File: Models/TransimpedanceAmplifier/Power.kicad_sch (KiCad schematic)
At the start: 0 parts

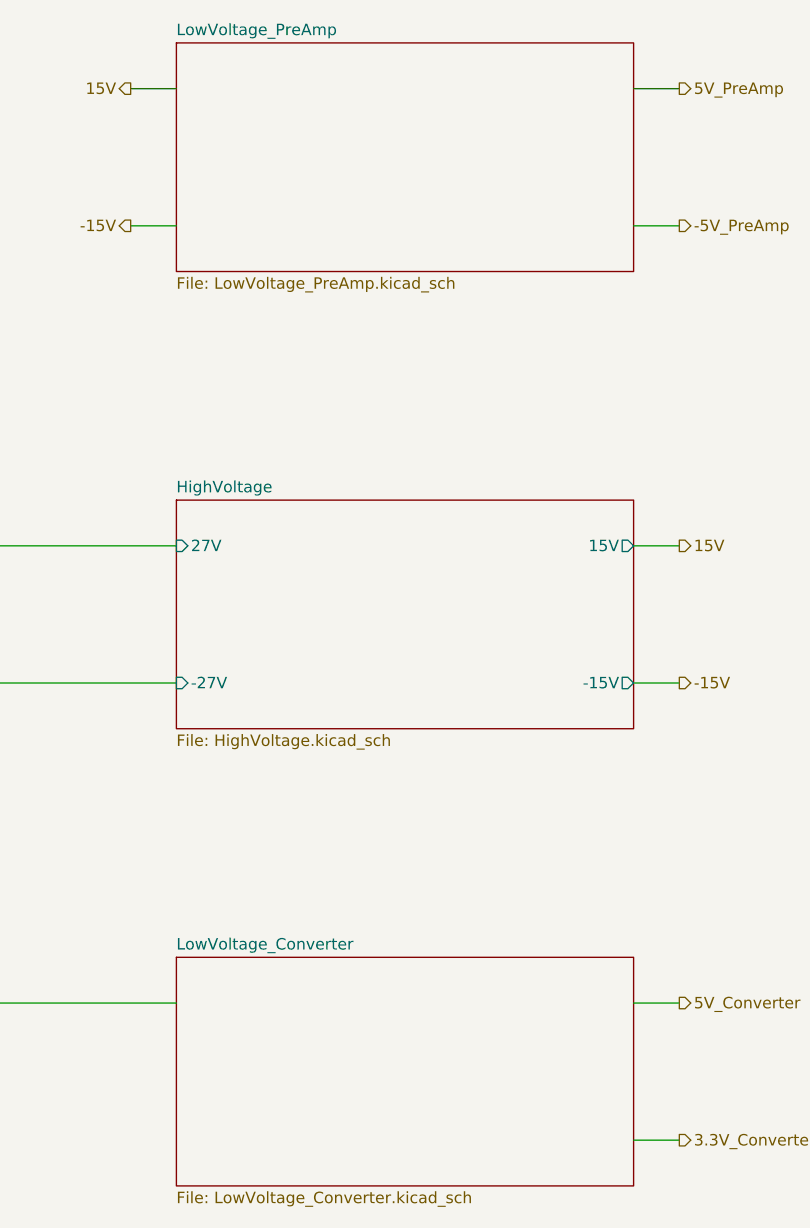
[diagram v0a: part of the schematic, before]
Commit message: Fully specified the high-level connections between subsystems
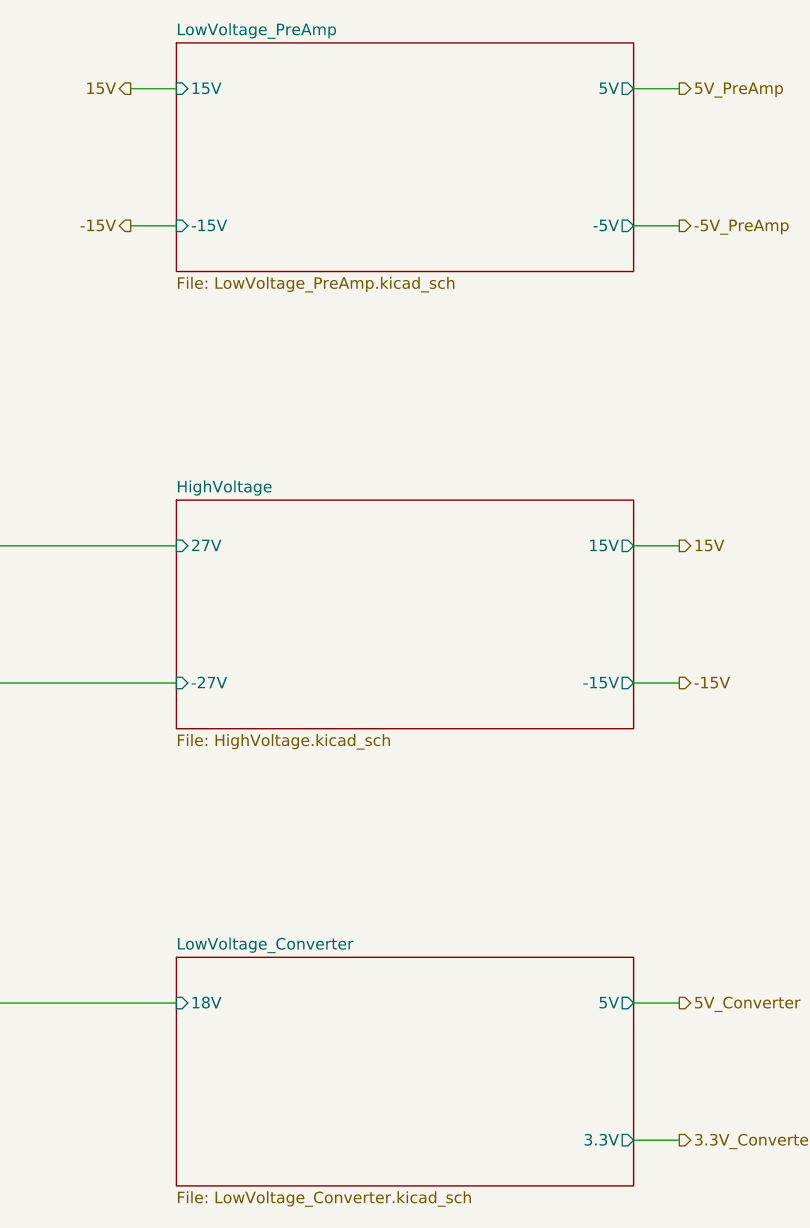
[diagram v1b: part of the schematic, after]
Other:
- sheet LowVoltage_Converter ports: added 18V, 3.3V, 5V; removed none
- sheet LowVoltage_PreAmp ports: added -15V, -5V, 15V, 5V; removed none
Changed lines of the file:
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@@
 		)
 		(instances
-			(project "TransimpedanceAmplifier"
-				(path "/ec9f2ae3-e40d-40eb-9760-2b611ee8efd1/68e8bf39-bd36-49ed-a85c-9ce753018063"
-					(page "12")
+			(project ""
+				(path "/d0ece2d4-5b22-4822-ad0c-e2361683ec3d"
+					(page "")
+				)
+			)
+			(project "TransimpedanceAmplifier"
+				(path "/ec9f2ae3-e40d-40eb-9760-2b611ee8efd1/d0ece2d4-5b22-4822-ad0c-e2361683ec3d"
+					(page "10")
 				)
 			)
@@
 			)
 		)
-		(instances
-			(project "TransimpedanceAmplifier"
-				(path "/ec9f2ae3-e40d-40eb-9760-2b611ee8efd1/68e8bf39-bd36-49ed-a85c-9ce753018063"
-					(page "16")
+		(pin "3.3V" output
+			(at 203.2 147.32 0)
+			(effects
+				(font
+					(size 1.27 1.27)
+				)
+				(justify right)
+			)
+		)
+		(pin "5V" output
+			(at 203.2 132.08 0)
+			(effects
+				(font
+					(size 1.27 1.27)
+				)
+				(justify right)
+			)
+		)
+		(pin "18V" input
+			(at 152.4 132.08 180)
+			(effects
+				(font
+					(size 1.27 1.27)
+				)
+				(justify left)
+			)
+		)
+		(instances
+			(project ""
+				(path "/d0ece2d4-5b22-4822-ad0c-e2361683ec3d"
+					(page "")
+				)
+			)
+			(project "TransimpedanceAmplifier"
+				(path "/ec9f2ae3-e40d-40eb-9760-2b611ee8efd1/d0ece2d4-5b22-4822-ad0c-e2361683ec3d"
+					(page "11")
 				)
 			)
@@
 		)
 		(instances
-			(project "TransimpedanceAmplifier"
-				(path "/ec9f2ae3-e40d-40eb-9760-2b611ee8efd1/68e8bf39-bd36-49ed-a85c-9ce753018063"
-					(page "14")
+			(project ""
+				(path "/d0ece2d4-5b22-4822-ad0c-e2361683ec3d"
+					(page "")
+				)
+			)
+			(project "TransimpedanceAmplifier"
+				(path "/ec9f2ae3-e40d-40eb-9760-2b611ee8efd1/d0ece2d4-5b22-4822-ad0c-e2361683ec3d"
+					(page "3")
 				)
 			)
@@
 			)
 		)
-		(instances
-			(project "TransimpedanceAmplifier"
-				(path "/ec9f2ae3-e40d-40eb-9760-2b611ee8efd1/68e8bf39-bd36-49ed-a85c-9ce753018063"
-					(page "15")
-				)
-			)
+		(pin "-5V" output
+			(at 203.2 45.72 0)
+			(effects
+				(font
+					(size 1.27 1.27)
+				)
+				(justify right)
+			)
+		)
+		(pin "-15V" input
+			(at 152.4 45.72 180)
+			(effects
+				(font
+					(size 1.27 1.27)
+				)
+				(justify left)
+			)
+		)
+		(pin "5V" output
+			(at 203.2 30.48 0)
+			(effects
+				(font
+					(size 1.27 1.27)
+				)
+				(justify right)
+			)
+		)
+		(pin "15V" input
+			(at 152.4 30.48 180)
+			(effects
+				(font
+					(size 1.27 1.27)
+				)
+				(justify left)
+			)
+		)
+		(instances
+			(project ""
+				(path "/d0ece2d4-5b22-4822-ad0c-e2361683ec3d"
+					(page "")
+				)
+			)
+			(project "TransimpedanceAmplifier"
+				(path "/ec9f2ae3-e40d-40eb-9760-2b611ee8efd1/d0ece2d4-5b22-4822-ad0c-e2361683ec3d"
+					(page "4")
+				)
+			)

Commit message: Syncing changes?
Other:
- note added: "Loads on Each Regulator 5 V (PreAmp) 13-17 mA 132-166 mW -5 V (PreAmp) 12-15 mA 117-153 mW 15 V 45-50 mA 616-687 mW -15 V 47-49 mA 597-650 mW 5 V (Converter) 37-40 mA 469-508 mW 3.3 V (Converter) 23 mA 49 mW"
- note added: "Maximum Permitted Power Dissipation Ambient Temperature: 30°C LM78L, TO-92 0.68 W 0.84 W (heat sinked) ~158.7°C/W (in a standard test PCB) LM78, TO-220 1.78 W 7.88 W (heat sinked) ~23.9°C/W (in a standard test PCB)"
- note removed: "TODO: Tabulate the maximum expected current at each regulator, to see whether LM78xx is needed anywhere instead of LM78Lxx"
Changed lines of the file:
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@@
 	(generator_version "9.0")
 	(paper "A4")
-	(text "TODO: Tabulate the maximum expected\ncurrent at each regulator, to see\nwhether LM78xx is needed anywhere\ninstead of LM78Lxx"
+	(text "Loads on Each Regulator\n\n5 V (PreAmp)\n13-17 mA\n132-166 mW\n\n-5 V (PreAmp)\n12-15 mA\n117-153 mW\n\n15 V\n45-50 mA\n616-687 mW\n\n-15 V\n47-49 mA\n597-650 mW\n\n5 V (Converter)\n37-40 mA\n469-508 mW\n\n3.3 V (Converter)\n23 mA\n49 mW\n"
 		(exclude_from_sim no)
-		(at 51.562 30.226 0)
+		(at 36.576 128.778 0)
 		(effects
 			(font
 				(size 1.27 1.27)
 			)
-			(justify left)
+			(justify left top)
 		)
 	)
+	(text "Maximum Permitted Power Dissipation\nAmbient Temperature: 30°C\n\nLM78L, TO-92\n0.68 W\n0.84 W (heat sinked)\n~158.7°C/W (in a standard test PCB)\n\nLM78, TO-220\n1.78 W\n7.88 W (heat sinked)\n~23.9°C/W (in a standard test PCB)"
+		(exclude_from_sim no)
+		(at 76.962 129.032 0)
+		(effects
+			(font
+				(size 1.27 1.27)
+			)
+			(justify left top)
+		)
+	)

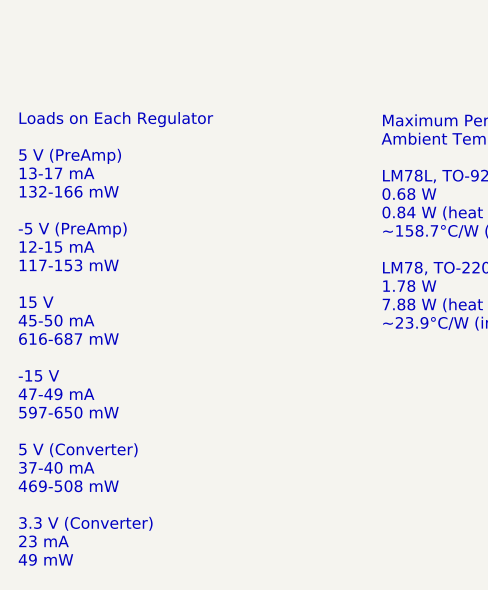
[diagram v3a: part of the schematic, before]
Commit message: Corrected some errors in the power calculations
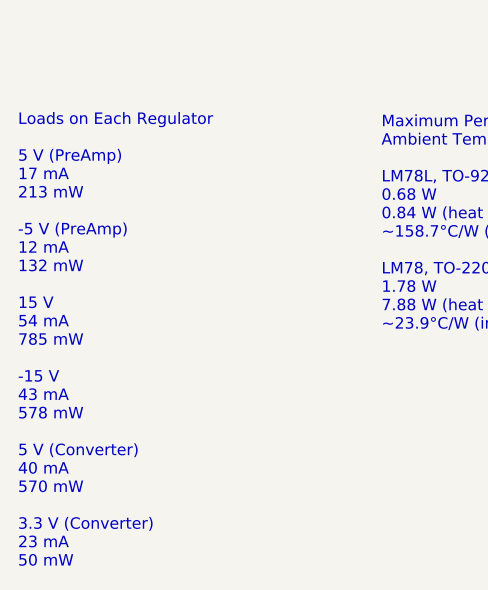
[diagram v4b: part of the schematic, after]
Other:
- note added: "Loads on Each Regulator 5 V (PreAmp) 17 mA 213 mW -5 V (PreAmp) 12 mA 132 mW 15 V 54 mA 785 mW -15 V 43 mA 578 mW 5 V (Converter) 40 mA 570 mW 3.3 V (Converter) 23 mA 50 mW"
- note removed: "Loads on Each Regulator 5 V (PreAmp) 13-17 mA 132-166 mW -5 V (PreAmp) 12-15 mA 117-153 mW 15 V 45-50 mA 616-687 mW -15 V 47-49 mA 597-650 mW 5 V (Converter) 37-40 mA 469-508 mW 3.3 V (Converter) 23 mA 49 mW"
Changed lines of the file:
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@@
 	(generator_version "9.0")
 	(paper "A4")
-	(text "Loads on Each Regulator\n\n5 V (PreAmp)\n13-17 mA\n132-166 mW\n\n-5 V (PreAmp)\n12-15 mA\n117-153 mW\n\n15 V\n45-50 mA\n616-687 mW\n\n-15 V\n47-49 mA\n597-650 mW\n\n5 V (Converter)\n37-40 mA\n469-508 mW\n\n3.3 V (Converter)\n23 mA\n49 mW\n"
+	(text "Loads on Each Regulator\n\n5 V (PreAmp)\n17 mA\n213 mW\n\n-5 V (PreAmp)\n12 mA\n132 mW\n\n15 V\n54 mA\n785 mW\n\n-15 V\n43 mA\n578 mW\n\n5 V (Converter)\n40 mA\n570 mW\n\n3.3 V (Converter)\n23 mA\n50 mW\n"
 		(exclude_from_sim no)
 		(at 36.576 128.778 0)

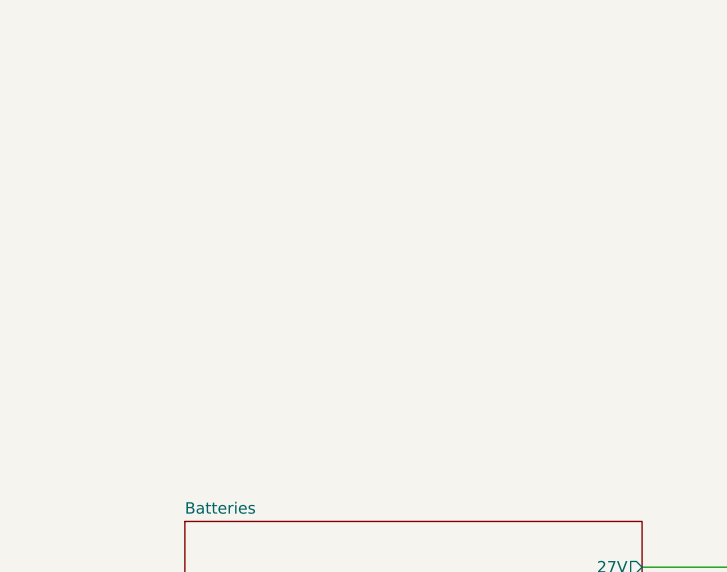
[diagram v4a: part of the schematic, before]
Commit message: Removed all protection diodes for now
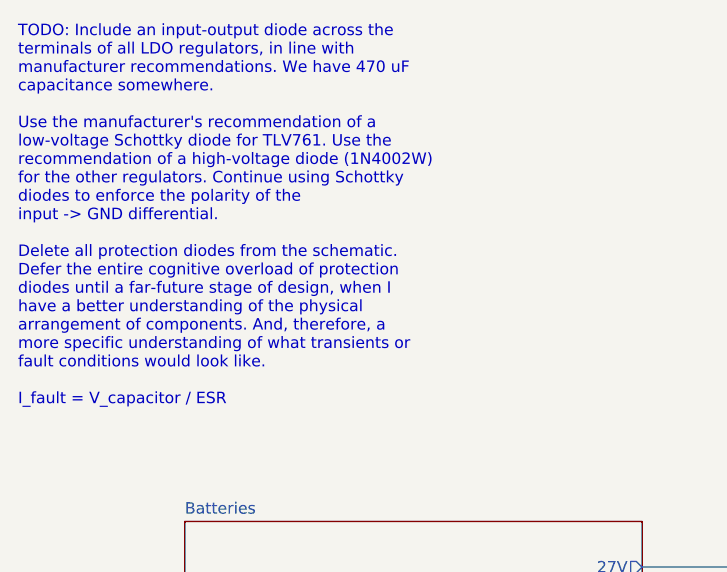
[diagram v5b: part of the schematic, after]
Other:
- note added: "TODO: Include an input-output diode across the terminals of all LDO regulators, in line with manufacturer recommendations. We have 470 uF capacitance somewhere. Use the manufacturer's recommendation of a low-voltage Schottky diode for TLV761. Use the recommendation of a high-voltage diode (1N4002W) for the other regulators. Continue using Schottky diodes to enforce the polarity of the input -> GN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"
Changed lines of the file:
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@@
 	(generator_version "9.0")
 	(paper "A4")
+	(text "TODO: Include an input-output diode across the\nterminals of all LDO regulators, in line with\nmanufacturer recommendations. We have 470 uF\ncapacitance somewhere.\n\nUse the manufacturer's recommendation of a\nlow-voltage Schottky diode for TLV761. Use the\nrecommendation of a high-voltage diode (1N4002W)\nfor the other regulators. Continue using Schottky\ndiodes to enforce the polarity of the\ninput -> GND differential.\n\nDelete all protection diodes from the schematic.\nDefer the entire cognitive overload of protection\ndiodes until a far-future stage of design, when I\nhave a better understanding of the physical\narrangement of components. And, therefore, a\nmore specific understanding of what transients or\nfault conditions would look like.\n\nI_fault = V_capacitor / ESR"
+		(exclude_from_sim no)
+		(at 32.258 21.082 0)
+		(effects
+			(font
+				(size 1.27 1.27)
+			)
+			(justify left top)
+		)
+	)
 	(text "Loads on Each Regulator\n\n5 V (PreAmp)\n17 mA\n213 mW\n\n-5 V (PreAmp)\n12 mA\n132 mW\n\n15 V\n54 mA\n785 mW\n\n-15 V\n43 mA\n578 mW\n\n5 V (Converter)\n40 mA\n570 mW\n\n3.3 V (Converter)\n23 mA\n50 mW\n"
 		(exclude_from_sim no)

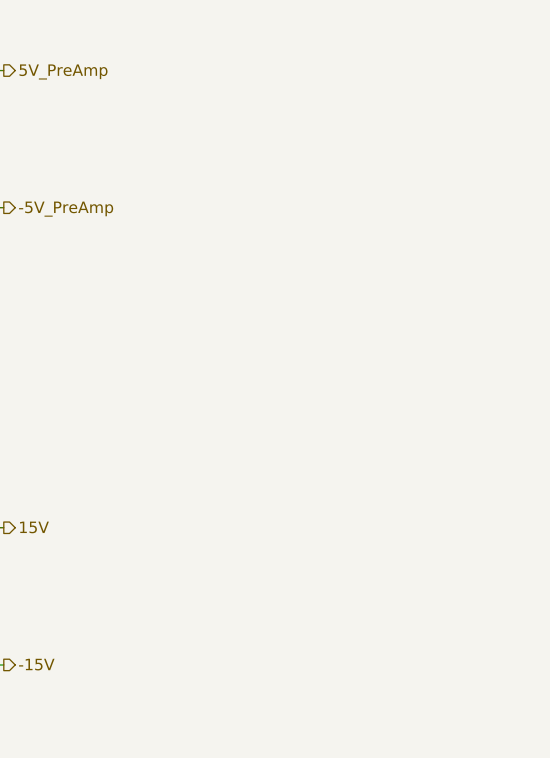
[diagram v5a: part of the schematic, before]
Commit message: Deleted all schematics for voltage regulators
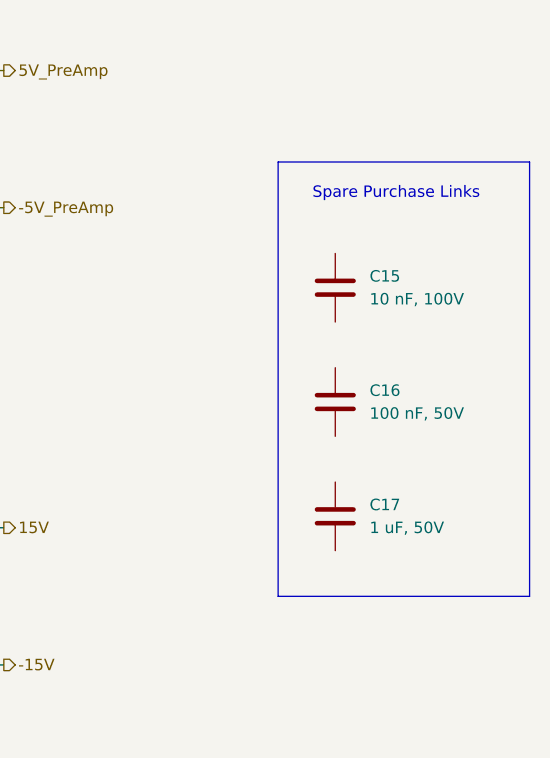
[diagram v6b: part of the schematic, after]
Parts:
- added C15: 10 nF, 100V, symbol Device:C
- added C16: 100 nF, 50V, symbol Device:C
- added C17: 1 uF, 50V, symbol Device:C
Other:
- note added: "Spare Purchase Links"

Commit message: Going to figure out the bypass capacitors next
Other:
- note added: "TODO: Purchase links for regulators Purchase links for new trimpots (Y variant)"
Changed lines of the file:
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@@
+		)
+	)
+	(text "TODO:\nPurchase links for regulators\nPurchase links for new trimpots (Y variant)"
+		(exclude_from_sim no)
+		(at 107.442 61.976 0)
+		(effects
+			(font
+				(size 1.27 1.27)
+			)
+			(justify left top)
 		)
 	)
